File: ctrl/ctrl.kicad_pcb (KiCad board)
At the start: 2 copper layers, 66 x 49.5 mm, 21 parts, among them J1 Conn_01x05_Pin, Q1 BC817, U1 ESP-12F, U2 LD1117V33

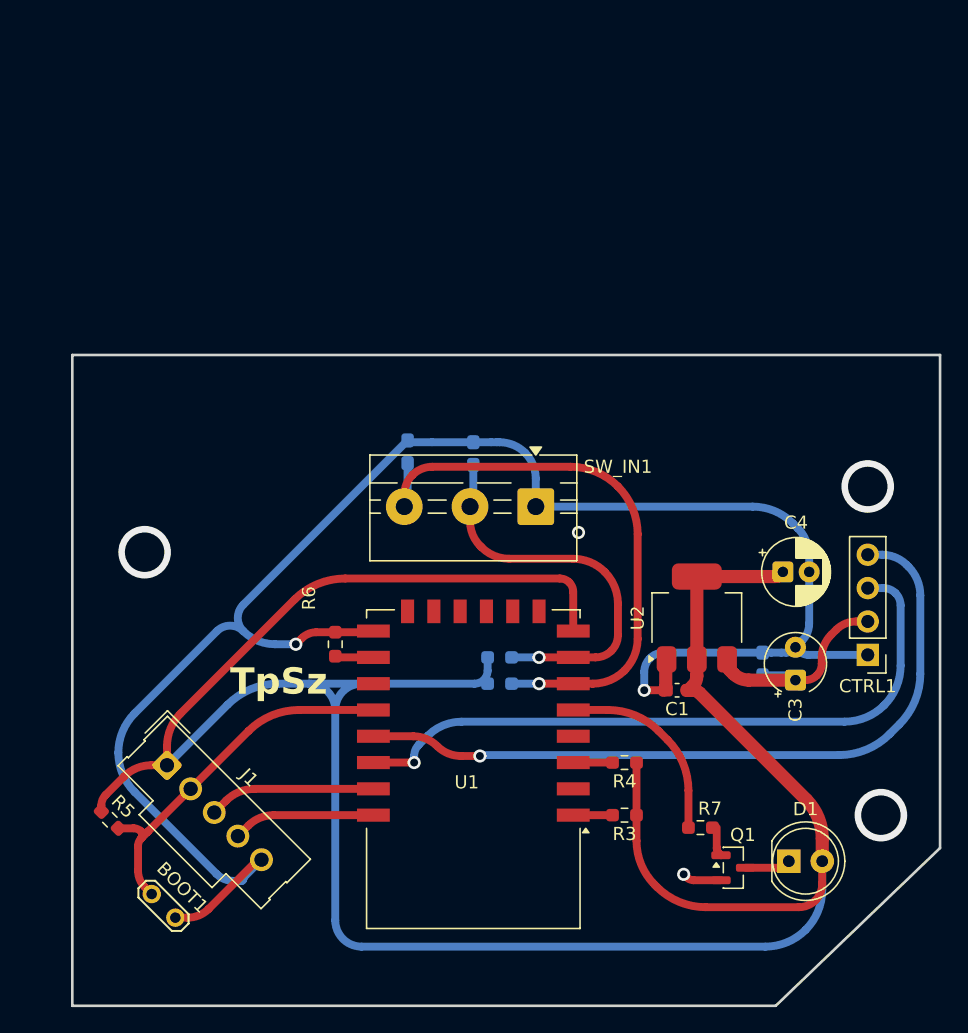
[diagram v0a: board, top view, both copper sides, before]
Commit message: PCB size was wrong, complete redesign...
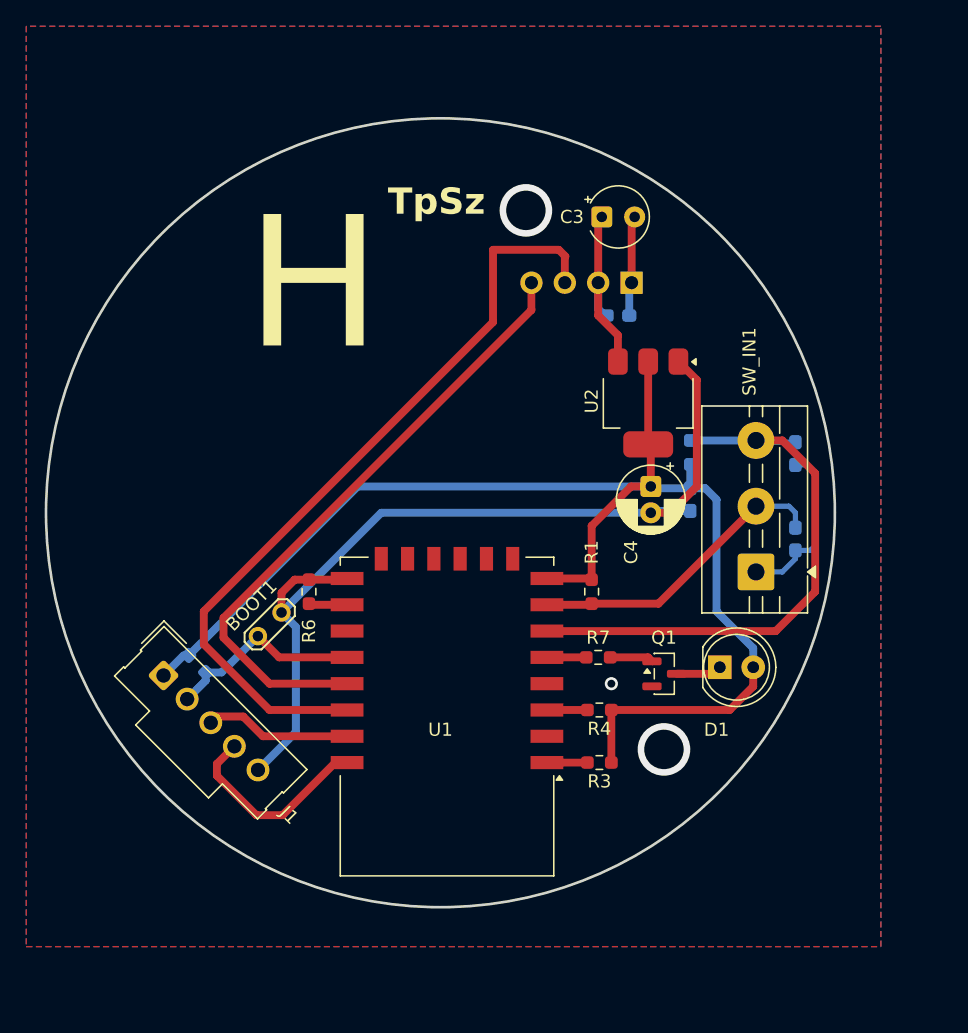
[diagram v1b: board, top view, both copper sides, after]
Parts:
- C1, CTRL1, R5: moved to B.Cu
- R1: moved to F.Cu
- moved C3 38.2 mm to (108.8, 79.5), turned to 0 degrees
- moved CTRL1 33.5 mm to (111.0, 84.5), turned to 90 degrees
- moved C6 29.5 mm to (123.5, 97.5), turned to -90 degrees
- moved C2 28.7 mm to (110.0, 87.0), turned to 0 degrees
- moved C5 25.3 mm to (123.5, 104.0), turned to -90 degrees
- moved R2 22.8 mm to (115.5, 97.4), turned to 90 degrees
- moved BOOT1 21.2 mm to (82.6, 111.4), turned to 45 degrees
- moved SW_IN1 17.5 mm to (120.5, 106.5), turned to 90 degrees
- moved U2 16.8 mm to (112.3, 93.7), turned to -90 degrees
- moved D1 15.7 mm to (117.8, 113.8)
- moved Q1 15.7 mm to (113.5, 114.2)
- moved R7 15.1 mm to (108.5, 113.0)
- moved C1 14.5 mm to (115.5, 101.0), turned to -90 degrees
- moved R5 13.6 mm to (78.0, 113.5)
- moved C4 12.0 mm to (112.5, 100.0), turned to -90 degrees
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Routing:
- net +3V3: track 200.6 -> 104.0 mm
- net GND: track 139.3 -> 89.9 mm, vias 4 -> 1
- net BOOT: track 29.0 -> 15.2 mm
- net IR: track 14.9 -> 2.99 mm
- net SSR_EN: track 57.1 -> 47.6 mm, vias 1 -> 0
- net RELAY_EN: track 52.0 -> 59.8 mm, vias 1 -> 0
- net DOWN: track 30.5 -> 23.4 mm, vias 1 -> 0
- net TX: track 10.8 -> 15.6 mm
- net +12V: track 17.3 -> 14.6 mm
- net RX: track 12.7 -> 11.2 mm
- net UP: track 45.6 -> 44.2 mm, vias 1 -> 0
- net Net-(Q1-B): track 2.21 -> 3.30 mm
- net (no net): vias 3 -> 2
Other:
- board size 66 x 49.5 mm -> 60 x 60 mm
- board text added: "H"
- board text added: "þ"
